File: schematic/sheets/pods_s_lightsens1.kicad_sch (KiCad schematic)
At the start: 4 parts, among them J2 SOIL-1x03

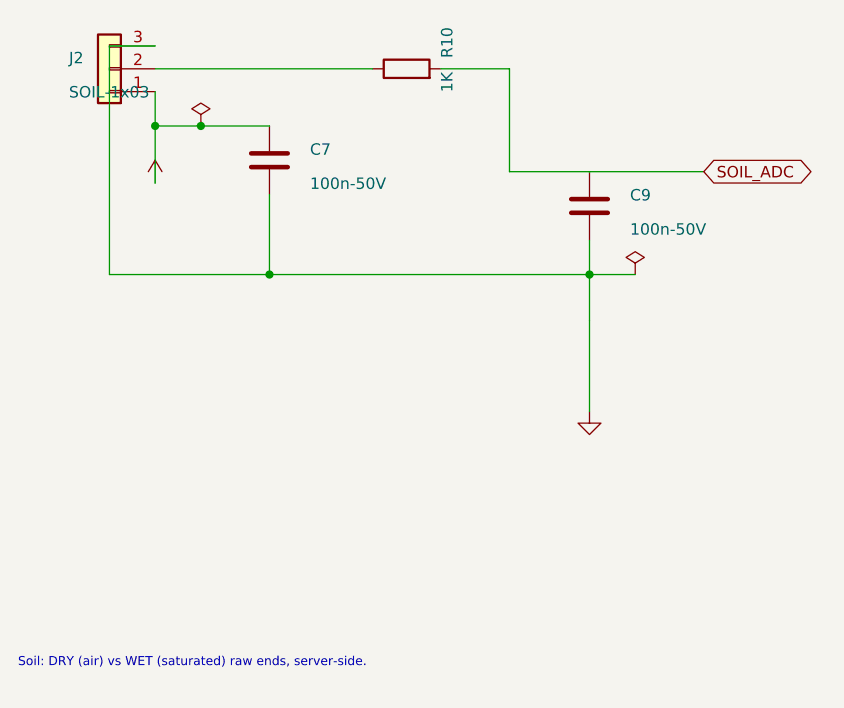
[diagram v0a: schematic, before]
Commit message: Organize schematic/: sheets/ mfg/ final/, drop sklib
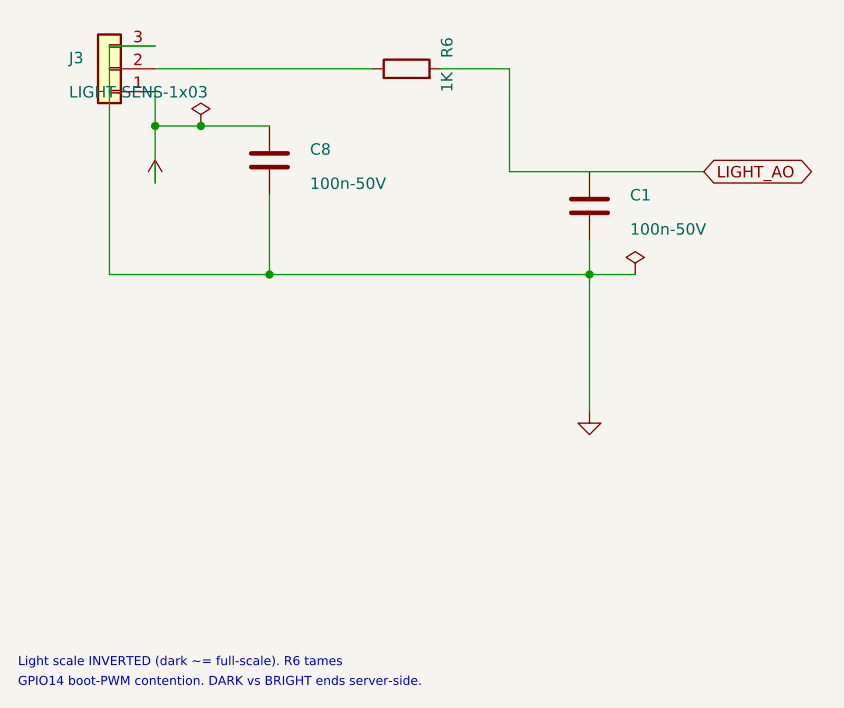
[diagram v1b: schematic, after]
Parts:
- removed C7, C9: 100n-50V, Capacitor_SMD:C_0603_1608Metric, symbol Device:C
- removed J2: SOIL-1x03, Connector_PinHeader_2.54mm:PinHeader_1x03_P2.54mm_Vertical, symbol Connector_Generic:Conn_01x03
- removed R10: 1K, Resistor_SMD:R_0603_1608Metric, symbol Device:R
- added C1, C8: 100n-50V, Capacitor_SMD:C_0603_1608Metric, symbol Device:C
- added J3: LIGHT-SENS-1x03, Connector_PinHeader_2.54mm:PinHeader_1x03_P2.54mm_Vertical, symbol Connector_Generic:Conn_01x03
- added R6: 1K, Resistor_SMD:R_0603_1608Metric, symbol Device:R
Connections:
- net +3V3: now also C8.1, J3.1 (Pin_1)
- net GND: now also C1.2, C8.2, J3.3 (Pin_3)
- new net: J3.2 (Pin_2), R6.1
- new net LIGHT_AO: C1.1, R6.2
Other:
- note added: "GPIO14 boot-PWM contention. DARK vs BRIGHT ends server-side."
- note added: "Light scale INVERTED (dark ~= full-scale). R6 tames"
- note removed: "Soil: DRY (air) vs WET (saturated) raw ends, server-side."
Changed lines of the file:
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@@
     (dnp no)
     (fields_autoplaced no)
-    (property "Reference" "J2"
+    (property "Reference" "J3"
       (at 31.06 72.46 0)
       (effects (font (size 1.27 1.27)) (justify right)))
-    (property "Value" "SOIL-1x03"
+    (property "Value" "LIGHT-SENS-1x03"
       (at 31.06 76.26 0)
       (effects (font (size 1.27 1.27)) (justify right)))
@@
     (instances
       (project "GrowMate"
-        (path "/216fdad8-4006-4d85-8157-93191bd90b6a/27f304de-9c3e-5417-beaa-bbe8c764e41e"
-          (reference "J2")
+        (path "/216fdad8-4006-4d85-8157-93191bd90b6a/91ef9dad-ef34-5895-821c-1f97dfd4b1f0"
+          (reference "J3")
           (unit 1)))))
   (symbol
@@
     (dnp no)
     (fields_autoplaced no)
-    (property "Reference" "R10"
+    (property "Reference" "R6"
       (at 73.08 72.46 0)
       (effects (font (size 1.27 1.27)) (justify left)))
@@
     (instances
       (project "GrowMate"
-        (path "/216fdad8-4006-4d85-8157-93191bd90b6a/27f304de-9c3e-5417-beaa-bbe8c764e41e"
-          (reference "R10")
+        (path "/216fdad8-4006-4d85-8157-93191bd90b6a/91ef9dad-ef34-5895-821c-1f97dfd4b1f0"
+          (reference "R6")
           (unit 1)))))
   (symbol
@@
     (dnp no)
     (fields_autoplaced no)
-    (property "Reference" "C9"
+    (property "Reference" "C1"
       (at 93.4 87.7 0)
       (effects (font (size 1.27 1.27)) (justify left)))
@@
     (instances
       (project "GrowMate"
-        (path "/216fdad8-4006-4d85-8157-93191bd90b6a/27f304de-9c3e-5417-beaa-bbe8c764e41e"
-          (reference "C9")
+        (path "/216fdad8-4006-4d85-8157-93191bd90b6a/91ef9dad-ef34-5895-821c-1f97dfd4b1f0"
+          (reference "C1")
           (unit 1)))))
   (symbol
@@
     (dnp no)
     (fields_autoplaced no)
-    (property "Reference" "C7"
+    (property "Reference" "C8"
       (at 57.84 82.62 0)
       (effects (font (size 1.27 1.27)) (justify left)))
@@
     (instances
       (project "GrowMate"
-        (path "/216fdad8-4006-4d85-8157-93191bd90b6a/27f304de-9c3e-5417-beaa-bbe8c764e41e"
-          (reference "C7")
+        (path "/216fdad8-4006-4d85-8157-93191bd90b6a/91ef9dad-ef34-5895-821c-1f97dfd4b1f0"
+          (reference "C8")
           (unit 1)))))
   (symbol
@@
     (instances
       (project "GrowMate"
-        (path "/216fdad8-4006-4d85-8157-93191bd90b6a/27f304de-9c3e-5417-beaa-bbe8c764e41e"
+        (path "/216fdad8-4006-4d85-8157-93191bd90b6a/91ef9dad-ef34-5895-821c-1f97dfd4b1f0"
           (reference "#+3V301")
           (unit 1)))))
@@
     (instances
       (project "GrowMate"
-        (path "/216fdad8-4006-4d85-8157-93191bd90b6a/27f304de-9c3e-5417-beaa-bbe8c764e41e"
+        (path "/216fdad8-4006-4d85-8157-93191bd90b6a/91ef9dad-ef34-5895-821c-1f97dfd4b1f0"
           (reference "#PWR02")
           (unit 1)))))
@@
     (stroke (width 0.1524) (type default))
 )
-  (global_label "SOIL_ADC"
+  (global_label "LIGHT_AO"
     (shape bidirectional)
     (at 101.6 85.09 0)
@@
     (instances
       (project "GrowMate"
-        (path "/216fdad8-4006-4d85-8157-93191bd90b6a/27f304de-9c3e-5417-beaa-bbe8c764e41e"
+        (path "/216fdad8-4006-4d85-8157-93191bd90b6a/91ef9dad-ef34-5895-821c-1f97dfd4b1f0"
           (reference "#GND03")
           (unit 1)))))
@@
     (instances
       (project "GrowMate"
-        (path "/216fdad8-4006-4d85-8157-93191bd90b6a/27f304de-9c3e-5417-beaa-bbe8c764e41e"
+        (path "/216fdad8-4006-4d85-8157-93191bd90b6a/91ef9dad-ef34-5895-821c-1f97dfd4b1f0"
           (reference "#PWR04")
           (unit 1)))))
@@
   (junction (at 53.34 96.52) (diameter 0) (color 0 0 0 0)
 )
-  (text "Soil: DRY (air) vs WET (saturated) raw ends, server-side."
+  (text "Light scale INVERTED (dark ~= full-scale). R6 tames"
     (at 25.4 139.7 0)
     (effects (font (size 1.0 1.0)) (justify left))
 )
+  (text "GPIO14 boot-PWM contention. DARK vs BRIGHT ends server-side."
+    (at 25.4 141.9 0)
+    (effects (font (size 1.0 1.0)) (justify left))
+)
